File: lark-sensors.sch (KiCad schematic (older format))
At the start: 31 parts, among them IC1 MS5611-01BA03, IC2 MS5611-01BA03, IC3 BMP388, IC4 BMP388, J10 Conn_01x05-Connector_Generic, J2 Conn_01x05-Connector_Generic, J5 Conn_01x05-Connector_Generic, U4 MCP1700T-3302E_TT, U5 PCA9544AD, U7 HCLAxxE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

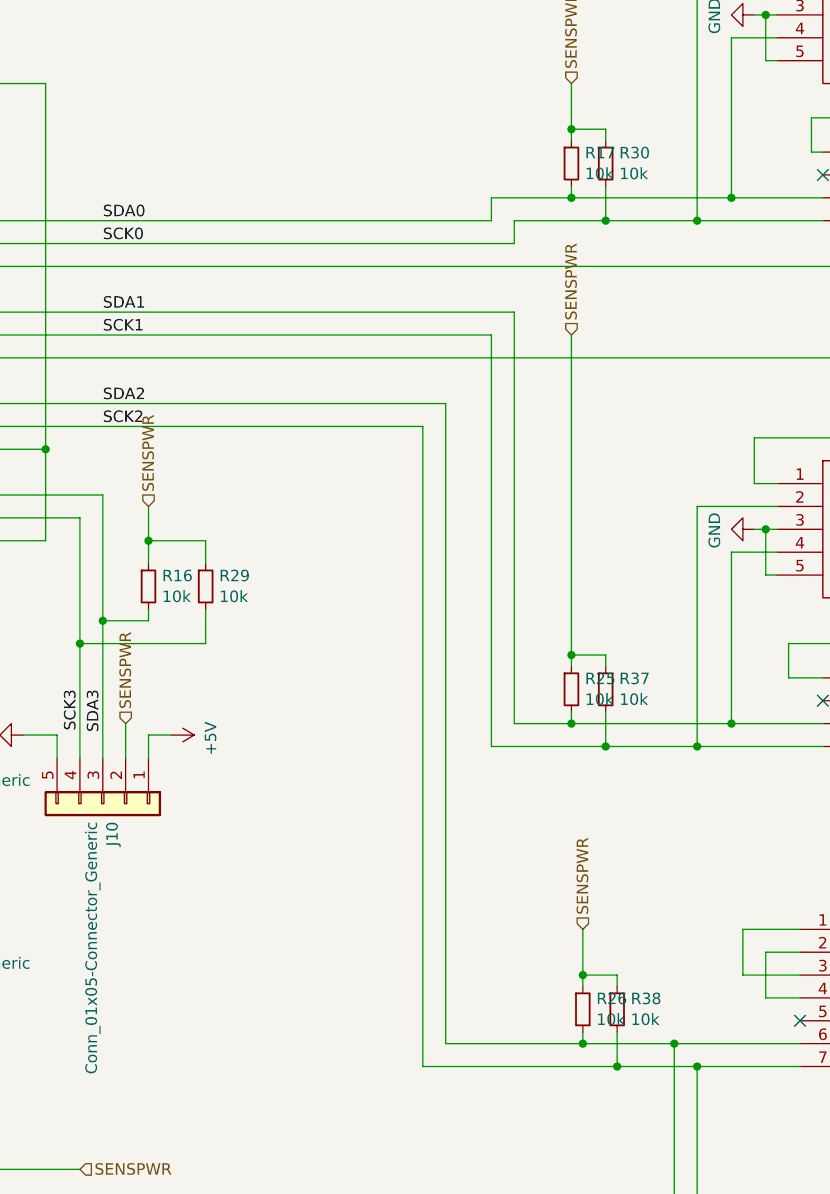
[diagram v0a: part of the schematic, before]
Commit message: change I2C pullups to 1k2
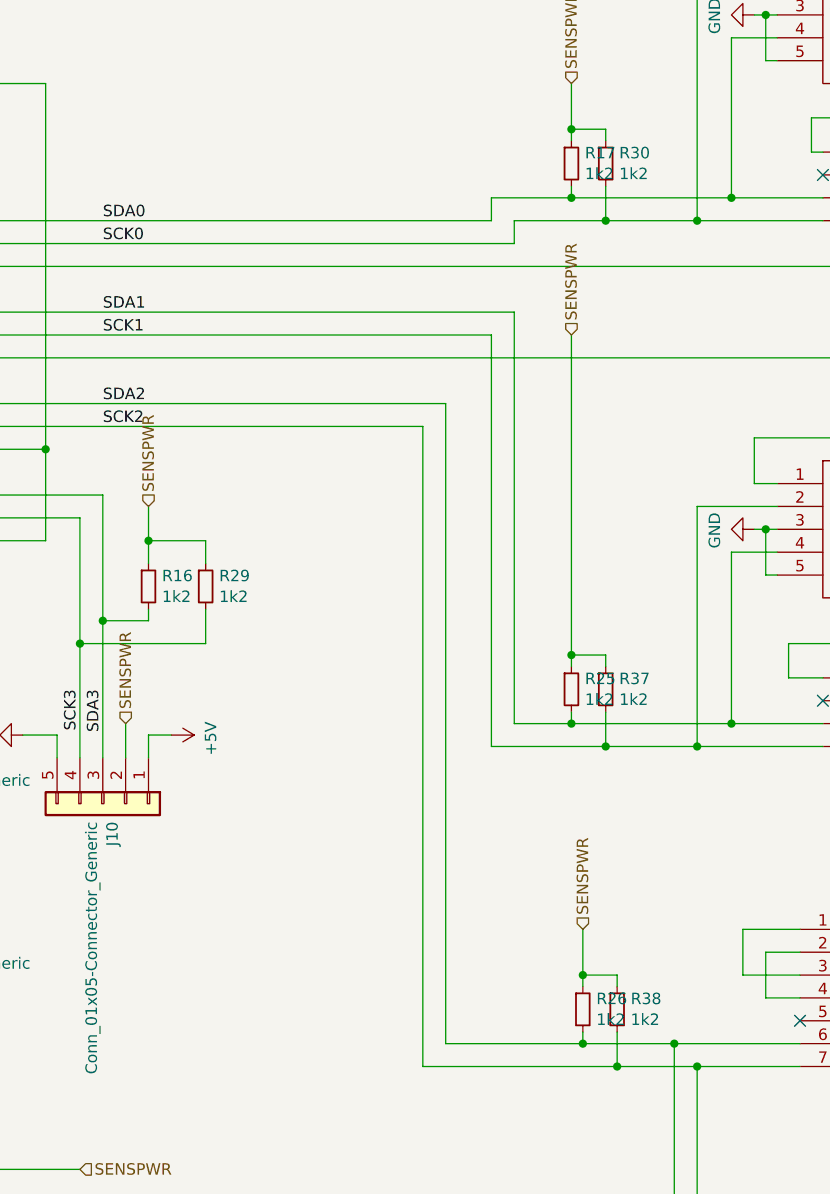
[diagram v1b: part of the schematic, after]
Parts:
- R16, R17, R25, R26, R29, R30, R37, R38: value 10k -> 1k2
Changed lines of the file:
@@
 P 4800 3900
 F 0 "R25" H 4859 3946 50  0000 L CNN
-F 1 "10k" H 4859 3855 50  0000 L CNN
+F 1 "1k2" H 4859 3855 50  0000 L CNN
 F 2 "Resistor_SMD:R_0805_2012Metric_Pad1.15x1.40mm_HandSolder" H 4800 3900 50  0001 C CNN
 F 3 "~" H 4800 3900 50  0001 C CNN
@@
 P 4950 3900
 F 0 "R37" H 5009 3946 50  0000 L CNN
-F 1 "10k" H 5009 3855 50  0000 L CNN
+F 1 "1k2" H 5009 3855 50  0000 L CNN
 F 2 "Resistor_SMD:R_0805_2012Metric_Pad1.15x1.40mm_HandSolder" H 4950 3900 50  0001 C CNN
 F 3 "~" H 4950 3900 50  0001 C CNN
@@
 P 4850 5300
 F 0 "R26" H 4909 5346 50  0000 L CNN
-F 1 "10k" H 4909 5255 50  0000 L CNN
+F 1 "1k2" H 4909 5255 50  0000 L CNN
 F 2 "Resistor_SMD:R_0805_2012Metric_Pad1.15x1.40mm_HandSolder" H 4850 5300 50  0001 C CNN
 F 3 "~" H 4850 5300 50  0001 C CNN
@@
 P 5000 5300
 F 0 "R38" H 5059 5346 50  0000 L CNN
-F 1 "10k" H 5059 5255 50  0000 L CNN
+F 1 "1k2" H 5059 5255 50  0000 L CNN
 F 2 "Resistor_SMD:R_0805_2012Metric_Pad1.15x1.40mm_HandSolder" H 5000 5300 50  0001 C CNN
 F 3 "~" H 5000 5300 50  0001 C CNN
@@
 P 4800 1600
 F 0 "R17" H 4859 1646 50  0000 L CNN
-F 1 "10k" H 4859 1555 50  0000 L CNN
+F 1 "1k2" H 4859 1555 50  0000 L CNN
 F 2 "Resistor_SMD:R_0805_2012Metric_Pad1.15x1.40mm_HandSolder" H 4800 1600 50  0001 C CNN
 F 3 "~" H 4800 1600 50  0001 C CNN
@@
 P 4950 1600
 F 0 "R30" H 5009 1646 50  0000 L CNN
-F 1 "10k" H 5009 1555 50  0000 L CNN
+F 1 "1k2" H 5009 1555 50  0000 L CNN
 F 2 "Resistor_SMD:R_0805_2012Metric_Pad1.15x1.40mm_HandSolder" H 4950 1600 50  0001 C CNN
 F 3 "~" H 4950 1600 50  0001 C CNN
@@
 P 2950 3450
 F 0 "R16" H 3009 3496 50  0000 L CNN
-F 1 "10k" H 3009 3405 50  0000 L CNN
+F 1 "1k2" H 3009 3405 50  0000 L CNN
 F 2 "Resistor_SMD:R_0805_2012Metric_Pad1.15x1.40mm_HandSolder" H 2950 3450 50  0001 C CNN
 F 3 "~" H 2950 3450 50  0001 C CNN
@@
 P 3200 3450
 F 0 "R29" H 3259 3496 50  0000 L CNN
-F 1 "10k" H 3259 3405 50  0000 L CNN
+F 1 "1k2" H 3259 3405 50  0000 L CNN
 F 2 "Resistor_SMD:R_0805_2012Metric_Pad1.15x1.40mm_HandSolder" H 3200 3450 50  0001 C CNN
 F 3 "~" H 3200 3450 50  0001 C CNN

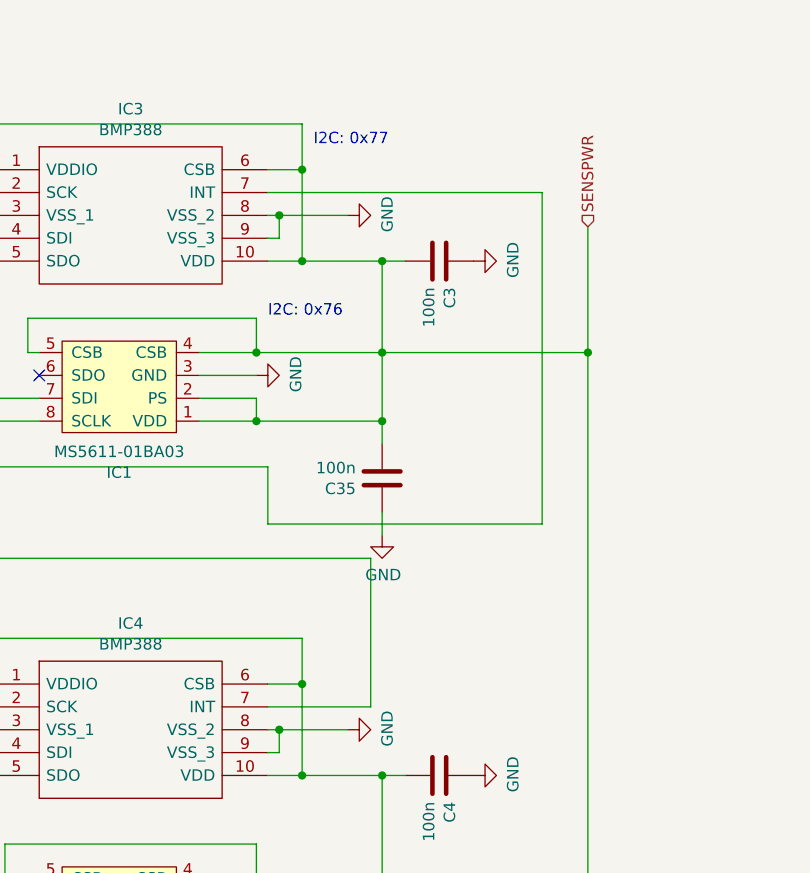
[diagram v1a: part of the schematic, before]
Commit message: add pullups to BMP388 INT lines
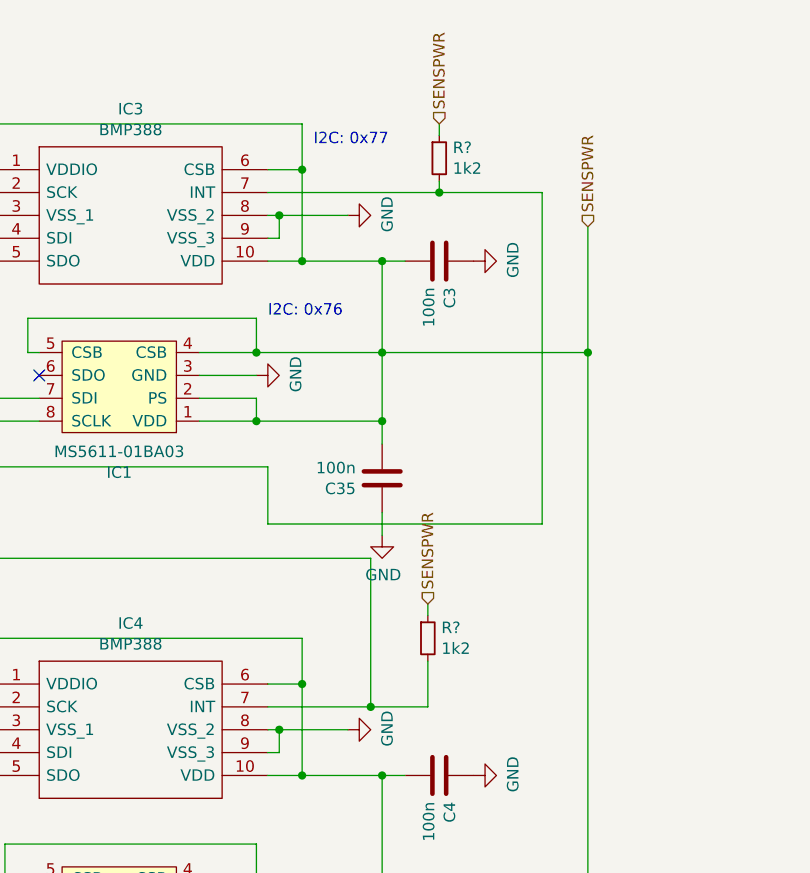
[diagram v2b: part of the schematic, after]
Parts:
- added R? (x2): 1k2, Resistor_SMD:R_0805_2012Metric_Pad1.15x1.40mm_HandSolder, symbol Device:R_Small
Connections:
- net SENSPWR: now also R?.1, R?.1
- net at IC3.7 (INT), U5.4 (~INT0): now also R?.2
- net at IC4.7 (INT), U5.7 (~INT1): now also R?.2
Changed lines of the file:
@@
 	8100 2300 8100 850
 Wire Wire Line
-	6900 850  8100 850
+	6900 850  7650 850
 Wire Wire Line
 	2500 2050 2500 2450
@@
 	600  4950 1050 4950
 Connection ~ 600  4150
+$Comp
+L Device:R_Small R?
+U 1 1 5CAB0101
+P 7650 700
+F 0 "R?" H 7709 746 50  0000 L CNN
+F 1 "1k2" H 7709 655 50  0000 L CNN
+F 2 "Resistor_SMD:R_0805_2012Metric_Pad1.15x1.40mm_HandSolder" H 7650 700 50  0001 C CNN
+F 3 "~" H 7650 700 50  0001 C CNN
+	1    7650 700
+	1    0    0    -1
+$EndComp
+$Comp
+L Device:R_Small R?
+U 1 1 5CAB0325
+P 7600 2800
+F 0 "R?" H 7659 2846 50  0000 L CNN
+F 1 "1k2" H 7659 2755 50  0000 L CNN
+F 2 "Resistor_SMD:R_0805_2012Metric_Pad1.15x1.40mm_HandSolder" H 7600 2800 50  0001 C CNN
+F 3 "~" H 7600 2800 50  0001 C CNN
+	1    7600 2800
+	1    0    0    -1
+$EndComp
+Text HLabel 7650 550  1    50   Input ~ 0
+SENSPWR
+Text HLabel 7600 2650 1    50   Input ~ 0
+SENSPWR
+Wire Wire Line
+	7350 3100 7600 3100
+Wire Wire Line
+	7600 3100 7600 2900
+Connection ~ 7350 3100
+Wire Wire Line
+	7600 2700 7600 2650
+Wire Wire Line
+	7650 850  7650 800
+Connection ~ 7650 850
+Wire Wire Line
+	7650 850  8100 850
+Wire Wire Line
+	7650 600  7650 550
 $EndSCHEMATC

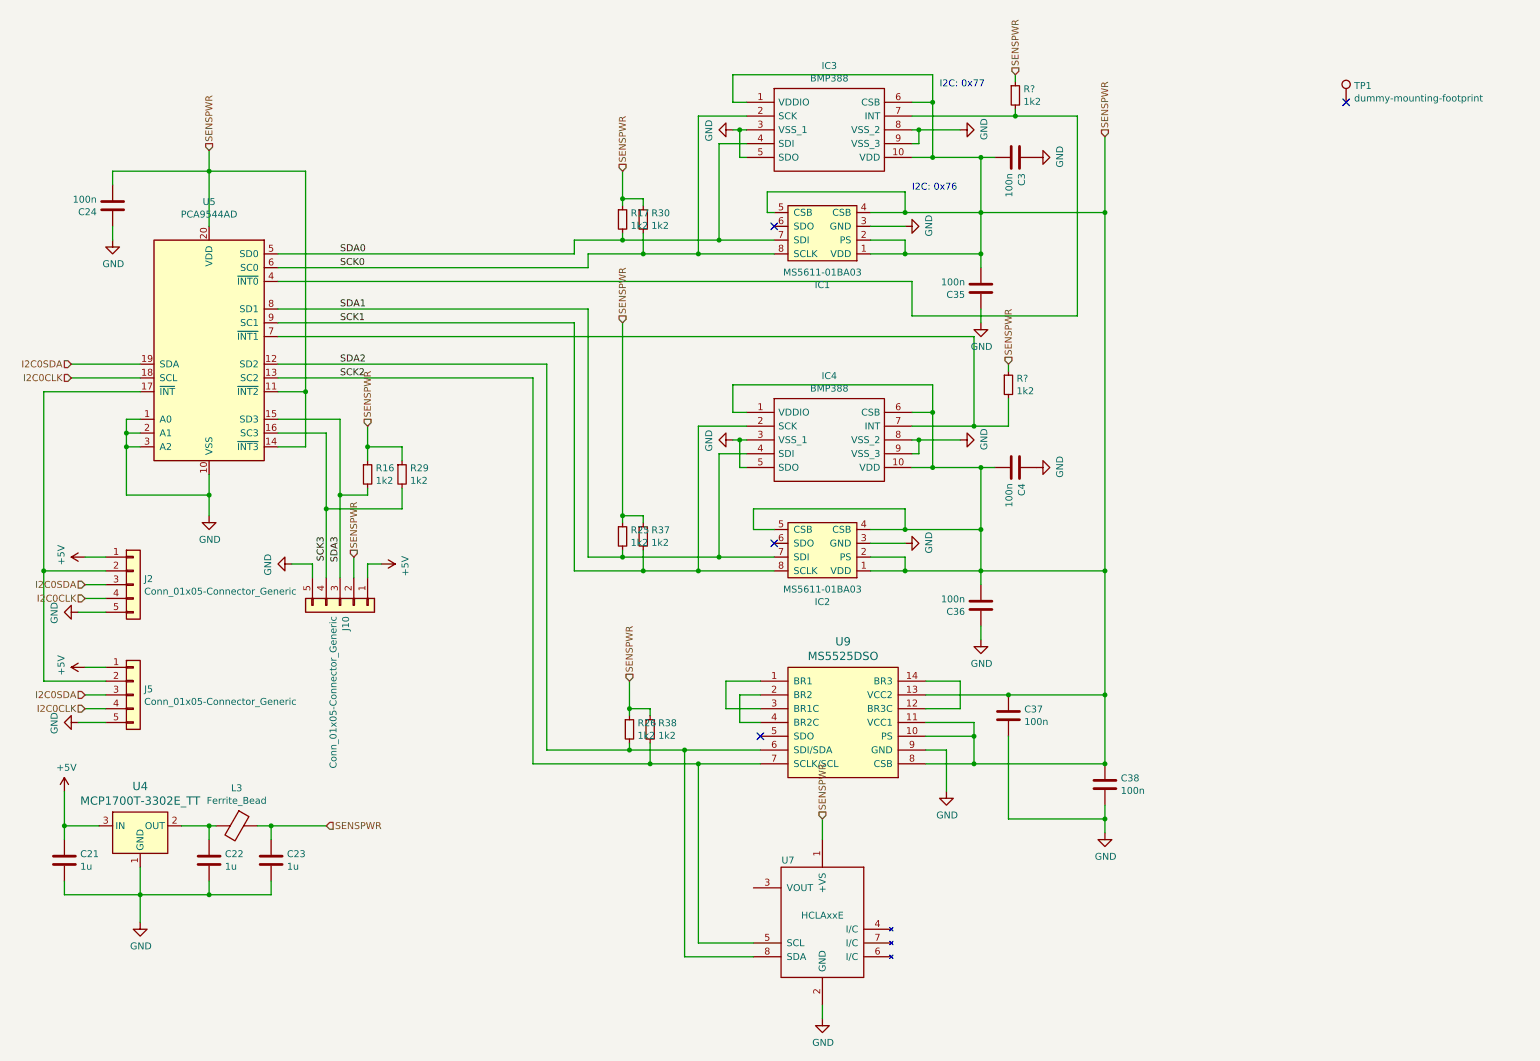
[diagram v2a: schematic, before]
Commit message: lark-sensors.sch: some cleanup
- tried kicad's bus feature
- replaced pullups by resistor array (this could be reverted
    to keeps things simpler)
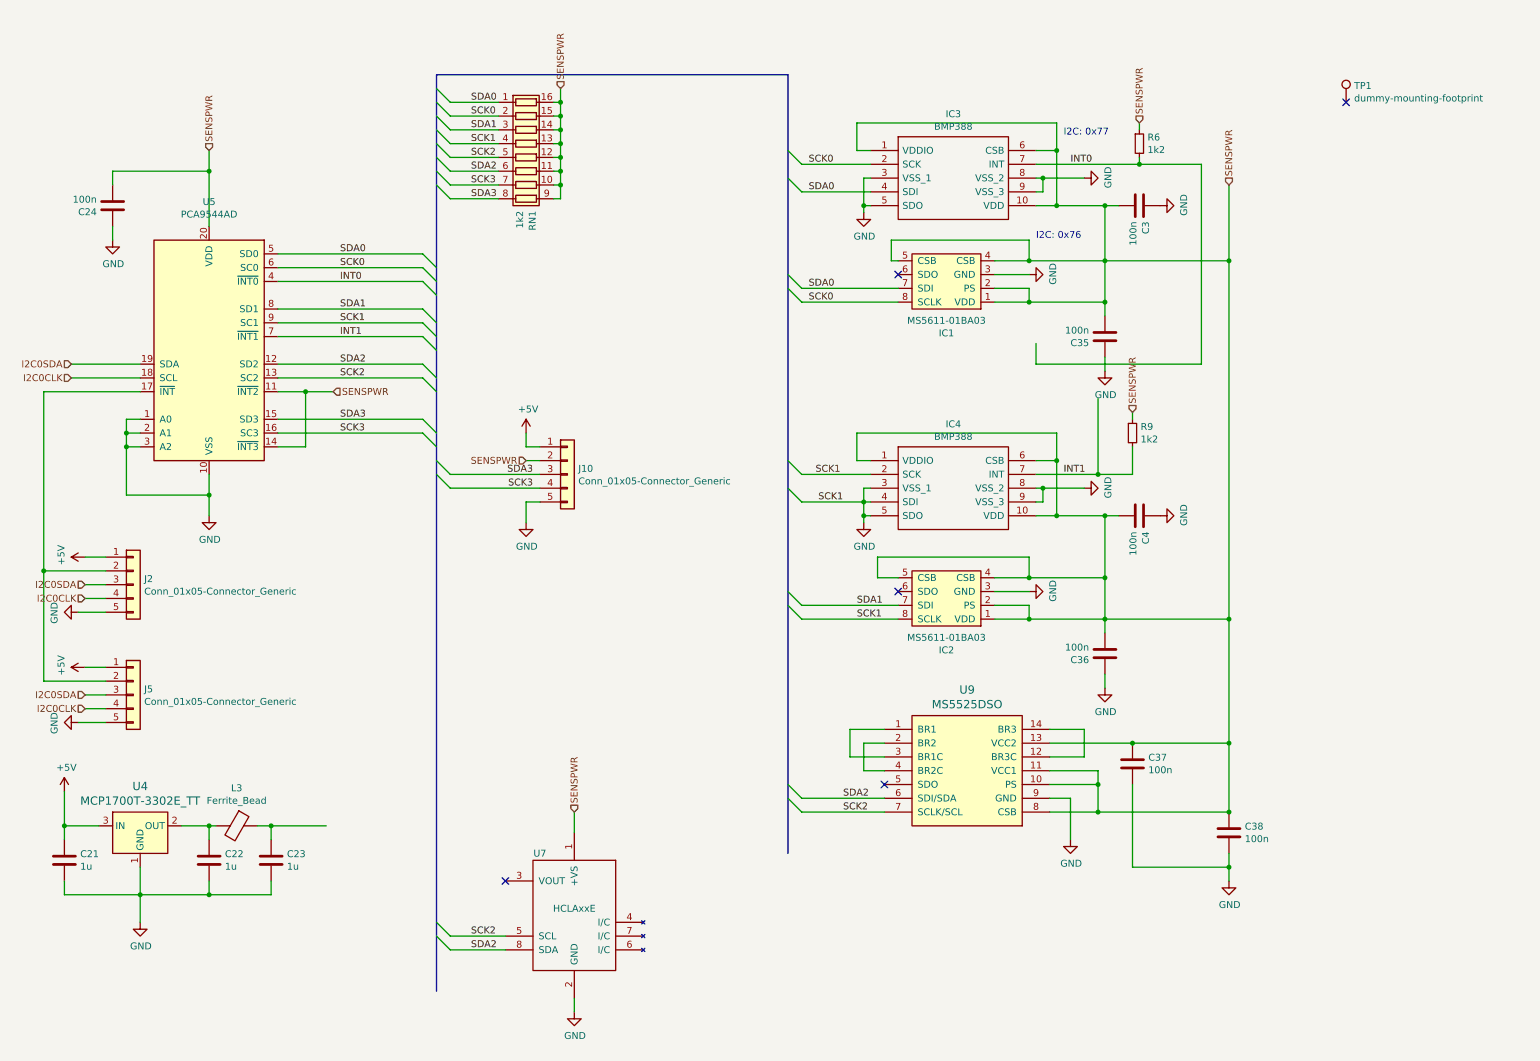
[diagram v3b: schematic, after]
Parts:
- removed R16, R17, R25, R26, R29, R30, R37, R38: 1k2, Resistor_SMD:R_0805_2012Metric_Pad1.15x1.40mm_HandSolder, symbol Device:R_Small
- added RN1: 1k2, symbol Device:R_Pack08
- gave numbers to parts that had none: 2
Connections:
- net SCK1 is gone; now on net GND: IC2.8 (SCLK), IC4.2 (SCK), U5.9 (SC1)
- net GND: now also IC4.4 (SDI), RN1.4 (R4.1)
- net SCK0: now also RN1.2 (R2.1)
- net SCK2: now also RN1.5 (R5.1)
- net SCK3: now also RN1.7 (R7.1)
- net SDA0: now also RN1.1 (R1.1)
- net SDA1: now also RN1.3 (R3.1); no longer IC4.4 (SDI)
- net SDA2: now also RN1.6 (R6.1)
- net SDA3: now also RN1.8 (R8.1)
- net SENSPWR: now also RN1.10 (R7.2), RN1.11 (R6.2), RN1.12 (R5.2), RN1.13 (R4.2), RN1.14 (R3.2), RN1.15 (R2.2), RN1.16 (R1.2), RN1.9 (R8.2); no longer C23.1, L3.1
- net INT0: now reaches IC3.7 (INT), R6.2, U5.4 (~INT0)
- net INT1: now reaches IC4.7 (INT), R9.2, U5.7 (~INT1)
- new net: C23.1, L3.1
- no-connect marks 4 -> 5
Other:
- moved on the sheet: C3, C35, C36, C37, C38, C4, IC1, IC2, IC3, IC4, J10, R6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
